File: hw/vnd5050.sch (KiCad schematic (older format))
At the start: 11 parts, among them U401 VND5050AJTR-E

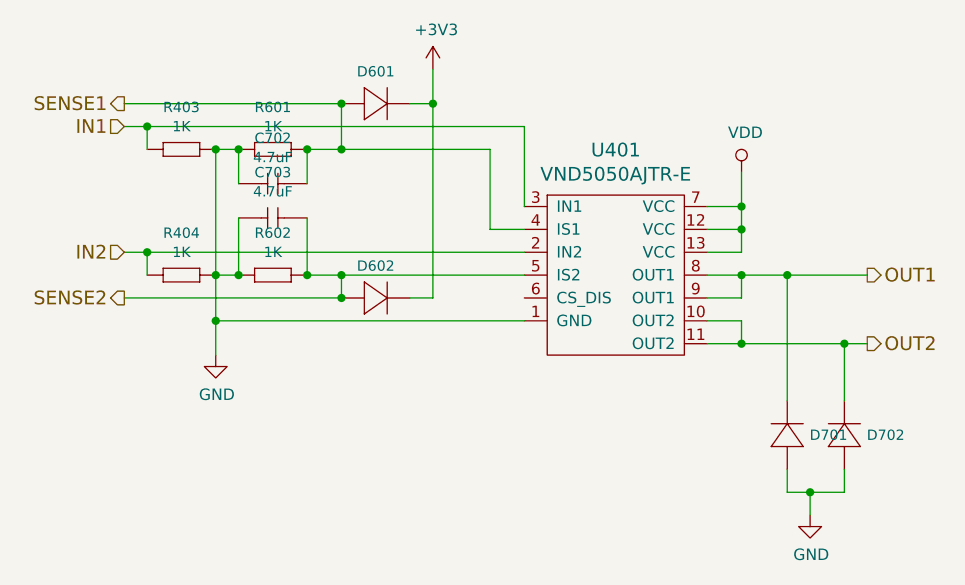
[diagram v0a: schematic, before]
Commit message: sense protection diodes replaced to zeners
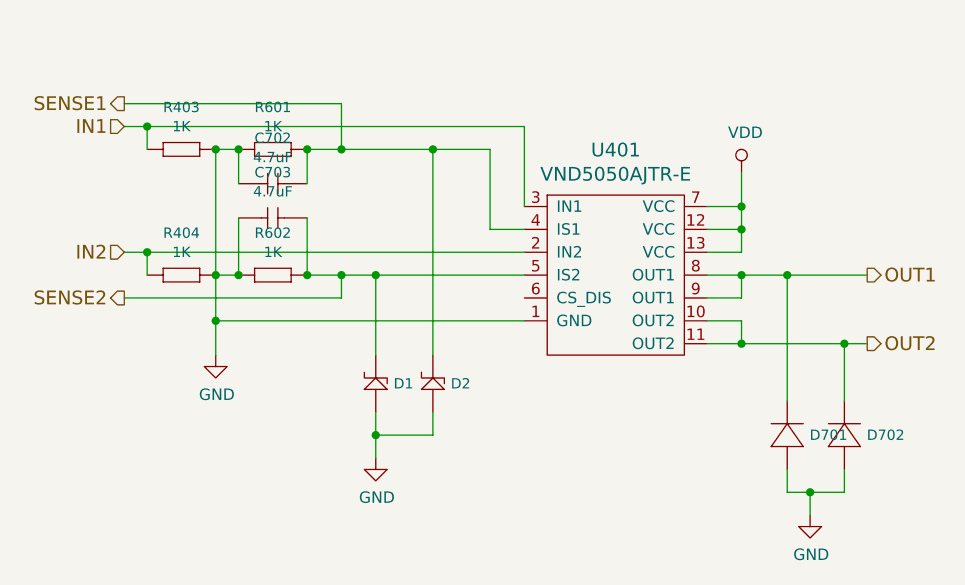
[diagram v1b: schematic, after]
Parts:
- removed D601, D602: DIODE_RS07J-GS18, usevolt:DO219AB, symbol usevolt:DIODE_RS07J-GS18
- added D1, D2: ZENER_MM3Z3V6T1G, usevolt:SOD-323, symbol usevolt:ZENER_MM3Z3V6T1G
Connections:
- net GND: now also D1.2, D2.2
- net SENSE1: now also D2.1
- net SENSE2: now also D1.1
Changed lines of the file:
@@
 	2950 4100 2950 4300
 Wire Wire Line
-	3500 4100 4300 4100
+	3500 4100 3650 4100
 Wire Wire Line
-	3500 3550 4150 3550
+	3500 3550 3900 3550
 Wire Wire Line
 	2650 3450 4300 3450
@@
 Connection ~ 3050 4100
 $Comp
-L usevolt:DIODE_RS07J-GS18 D602
-U 1 1 5B239934
-P 3700 4200
-F 0 "D602" H 3650 4340 45  0000 C CNN
-F 1 "DIODE_RS07J-GS18" H 3720 4140 45  0001 L BNN
-F 2 "usevolt:DO219AB" H 3730 4350 20  0001 C CNN
-F 3 "http://www.vishay.com/docs/85742/rs07b.pdf" H 3720 4220 60  0001 C CNN
-F 4 "1864882" H 4320 4820 60  0001 C CNN "2nd Source Part Number"
-F 5 "Digi-Key" H 4020 4520 60  0001 C CNN "1st Source"
-F 6 "Farnell" H 4220 4720 60  0001 C CNN "2nd Source"
-F 7 "RS07J-GS18" H 3920 4420 60  0001 C CNN "Manufacturer Part Number"
-F 8 "RS07J-GS18-ND" H 4120 4620 60  0001 C CNN "1st Source Part Number"
-F 9 "Vishay Semiconductor Diodes Division" H 3820 4320 60  0001 C CNN "Manufacturer"
-	1    3700 4200
-	1    0    0    -1
+L usevolt:ZENER_MM3Z3V6T1G D1
+U 1 1 5BAA330C
+P 3650 4500
+F 0 "D1" V 3575 4422 45  0000 R CNN
+F 1 "ZENER_MM3Z3V6T1G" H 3925 4875 45  0001 L BNN
+F 2 "usevolt:SOD-323" H 3625 4875 20  0001 C CNN
+F 3 "http://www.mouser.com/ds/2/308/MM3Z2V4T1-D-269162.pdf" H 4000 5075 60  0001 C CNN
+F 4 "Mouser" H 3970 4820 60  0001 C CNN "1st Source"
+F 5 "MM3Z3V6T1G" H 3870 4720 60  0001 C CNN "Manufacturer Part Number"
+F 6 "863-MM3Z3V6T1G" H 4070 4920 60  0001 C CNN "1st Source Part Number"
+F 7 "ON Semiconductor" H 3925 4975 60  0001 C CNN "Manufacturer"
+	1    3650 4500
+	0    -1   -1   0
 $EndComp
-Connection ~ 3500 4200
 $Comp
-L usevolt:DIODE_RS07J-GS18 D601
-U 1 1 5B239A24
-P 3700 3350
-F 0 "D601" H 3650 3490 45  0000 C CNN
-F 1 "DIODE_RS07J-GS18" H 3720 3290 45  0001 L BNN
-F 2 "usevolt:DO219AB" H 3730 3500 20  0001 C CNN
-F 3 "http://www.vishay.com/docs/85742/rs07b.pdf" H 3720 3370 60  0001 C CNN
-F 4 "1864882" H 4320 3970 60  0001 C CNN "2nd Source Part Number"
-F 5 "Digi-Key" H 4020 3670 60  0001 C CNN "1st Source"
-F 6 "Farnell" H 4220 3870 60  0001 C CNN "2nd Source"
-F 7 "RS07J-GS18" H 3920 3570 60  0001 C CNN "Manufacturer Part Number"
-F 8 "RS07J-GS18-ND" H 4120 3770 60  0001 C CNN "1st Source Part Number"
-F 9 "Vishay Semiconductor Diodes Division" H 3820 3470 60  0001 C CNN "Manufacturer"
-	1    3700 3350
-	1    0    0    -1
+L usevolt:ZENER_MM3Z3V6T1G D2
+U 1 1 5BAA33EF
+P 3900 4500
+F 0 "D2" V 3825 4422 45  0000 R CNN
+F 1 "ZENER_MM3Z3V6T1G" H 4175 4875 45  0001 L BNN
+F 2 "usevolt:SOD-323" H 3875 4875 20  0001 C CNN
+F 3 "http://www.mouser.com/ds/2/308/MM3Z2V4T1-D-269162.pdf" H 4250 5075 60  0001 C CNN
+F 4 "Mouser" H 4220 4820 60  0001 C CNN "1st Source"
+F 5 "MM3Z3V6T1G" H 4120 4720 60  0001 C CNN "Manufacturer Part Number"
+F 6 "863-MM3Z3V6T1G" H 4320 4920 60  0001 C CNN "1st Source Part Number"
+F 7 "ON Semiconductor" H 4175 4975 60  0001 C CNN "Manufacturer"
+	1    3900 4500
+	0    -1   -1   0
 $EndComp
-Connection ~ 3500 3350
+Wire Wire Line
+	3900 4450 3900 3550
+Connection ~ 3900 3550
+Wire Wire Line
+	3900 3550 4150 3550
+Wire Wire Line
+	3650 4450 3650 4100
+Connection ~ 3650 4100
+Wire Wire Line
+	3650 4100 4300 4100
 $Comp
-L power:+3V3 #PWR0101
-U 1 1 5B239AE4
-P 3900 3200
-F 0 "#PWR0101" H 3900 3050 50  0001 C CNN
-F 1 "+3V3" H 3915 3373 50  0000 C CNN
-F 2 "" H 3900 3200 50  0000 C CNN
-F 3 "" H 3900 3200 50  0000 C CNN
-	1    3900 3200
+L power:GND #PWR0101
+U 1 1 5BAA4BC4
+P 3650 4900
+F 0 "#PWR0101" H 3650 4650 50  0001 C CNN
+F 1 "GND" H 3655 4727 50  0000 C CNN
+F 2 "" H 3650 4900 50  0000 C CNN
+F 3 "" H 3650 4900 50  0000 C CNN
+	1    3650 4900
 	1    0    0    -1
 $EndComp
 Wire Wire Line
-	3900 3200 3900 3350
+	3650 4900 3650 4800
 Wire Wire Line
-	3900 3350 3800 3350
+	3650 4800 3900 4800
 Wire Wire Line
-	3900 3350 3900 4200
+	3900 4800 3900 4700
+Connection ~ 3650 4800
 Wire Wire Line
-	3900 4200 3800 4200
-Connection ~ 3900 3350
+	3650 4800 3650 4700
 $EndSCHEMATC
